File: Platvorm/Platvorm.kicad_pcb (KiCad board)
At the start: 2 copper layers, 40.3 x 80 mm, 38 parts, among them J1 Power Header 2x8, J2 GPIO 2x14, J3 USB-C, Q1 S8050, Q2 S8050, SW1 BOOT, SW2 RESET, U1 ESP32-C6-WROOM-1-N8, U2 TPS54202DDCR, U3 USBLC6-2SC6, U4 CH340C

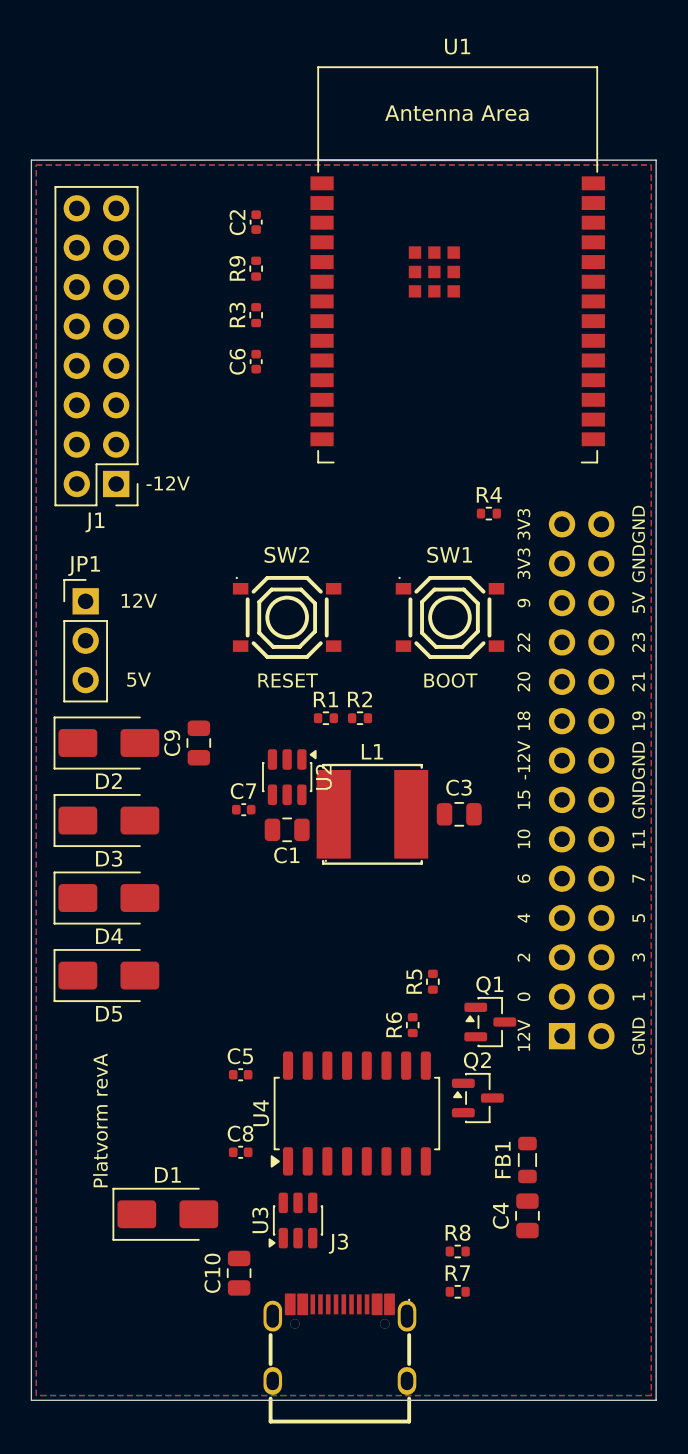
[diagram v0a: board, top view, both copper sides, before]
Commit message: Route board: DRC 0 violations, 0 unconnected
- freerouting pass (127 nets) + hand-finished stragglers:
  +5V to J2.24 (B.Cu row-band approach), IO22, +12V to JP1.1
  (via-hop x=56.6), +12V_RAW rerouted east (x=57.34), +5V west
  re-feed via B.Cu, CC lines, J3 GND tab bridges, C3 GND stitch via
- Default netclass clearance 0.2 -> 0.15mm (JLC 2-layer capability
  is 0.09mm; unlocks east-column lane capacity for J2 fanout)
- min_resolved_spokes 2 -> 1: four PTH GND pads (J2.14/28, J3 tabs)
  connect via 1 thermal spoke + PTH barrel + verified track ties
- Known deviation: SW node uses 2 vias + 5mm B.Cu jumper under U2
  (F.Cu corridor blocked by GND/FB/VOUT_PRE walls; ~4nH added loop
  inductance, acceptable at 500kHz with spread-spectrum TPS54202)
- Final: 576 tracks, 66 vias, 2013mm total, EN 69mm (was 103),
  IO9 67mm (was 85), GND pours filled both layers
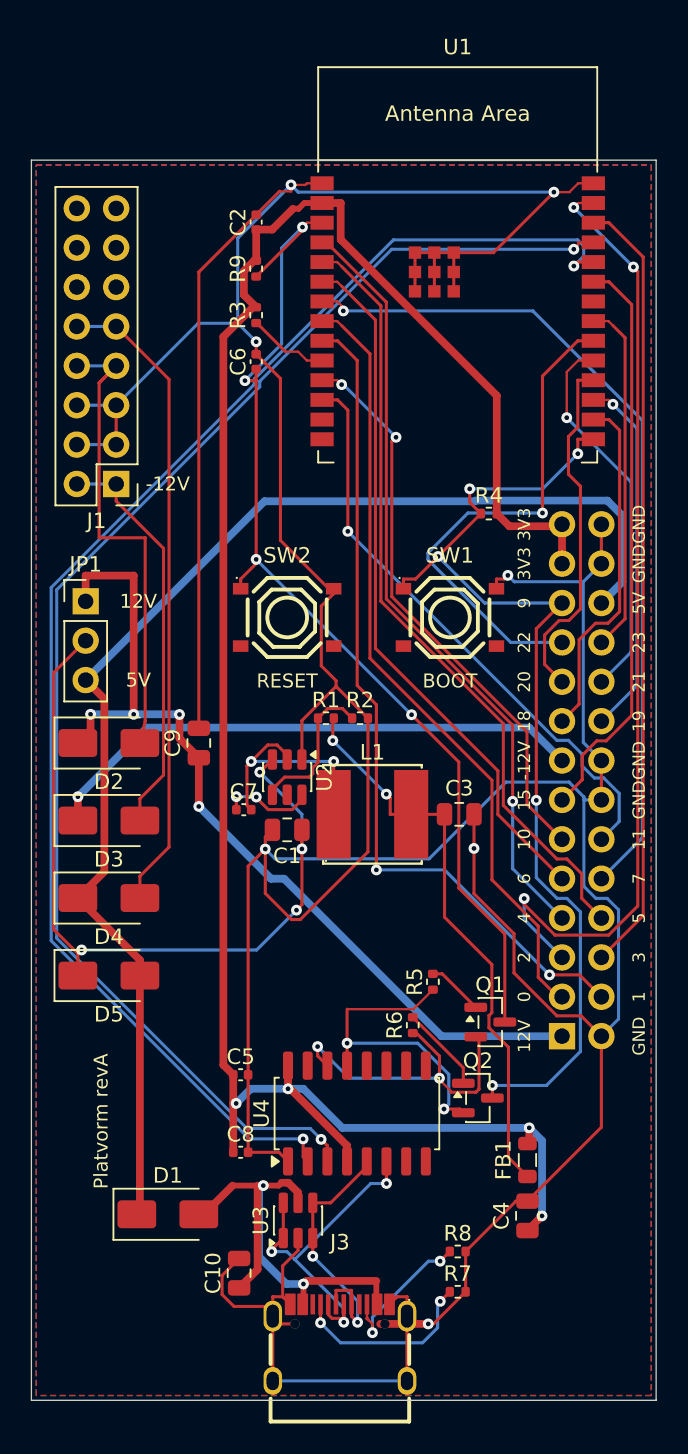
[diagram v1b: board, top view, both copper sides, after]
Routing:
- net GND: track 0.00 -> 333.0 mm, vias 0 -> 7
- net +3V3: track 0.00 -> 135.7 mm, vias 0 -> 4
- net U0RXD: track 0.00 -> 92.8 mm, vias 0 -> 2
- net U0TXD: track 0.00 -> 90.7 mm, vias 0 -> 2
- net +5V: track 0.00 -> 83.4 mm
- net EN: track 0.00 -> 69.0 mm, vias 0 -> 4
- net IO9: track 0.00 -> 66.9 mm, vias 0 -> 5
- net IO2: track 0.00 -> 62.3 mm, vias 0 -> 3
- net +12V: track 0.00 -> 57.7 mm, vias 0 -> 4
- net IO7: track 0.00 -> 54.6 mm, vias 0 -> 1
- net IO1: track 0.00 -> 54.1 mm, vias 0 -> 2
- net /Power Supply/VIN_BUCK: track 0.00 -> 50.9 mm, vias 0 -> 4
- net IO0: track 0.00 -> 50.7 mm
- net IO5: track 0.00 -> 50.7 mm
- net IO3: track 0.00 -> 50.4 mm
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
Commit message: Fab fixes: J3 shield tab annular/clearance, IO8 track width
- J3 USB-C shield tabs: height 0.7->0.8mm (annular 0.15mm = board min),
  pad clearance 0.1->0.2mm; clears 2 annular-width + 6 plane-clearance
  DRC errors against the +3V3 plane
- IO8 track: 0.1875->0.2mm; clears connection-width neck at U1.10
- 24 unconnected nets remain (routing WIP); DRC report in DRC5.rpt
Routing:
- net GND: track 333.0 -> 30.4 mm, vias 7 -> 28
- net +3V3: track 135.7 -> 10.5 mm, vias 4 -> 10
- net +5V: track 83.4 -> 160.2 mm, vias 0 -> 10
- net IO4: track 50.2 -> 1.80 mm
- net IO11: track 38.1 -> 0.00 mm, vias 1 -> 0
- net /Power Supply/VOUT_PRE: track 37.0 -> 7.90 mm
- net IO6: track 45.5 -> 70.9 mm, vias 0 -> 8
- net IO10: track 36.9 -> 60.6 mm, vias 2 -> 15
- net IO21: track 24.5 -> 1.80 mm
- net IO19: track 23.4 -> 1.80 mm
- net IO15: track 37.3 -> 57.3 mm, vias 0 -> 6
- net U0RXD: track 92.8 -> 75.3 mm, vias 2 -> 10
- net VBUS: track 31.2 -> 14.8 mm
- net /Power Supply/VIN_BUCK: track 50.9 -> 36.9 mm, vias 4 -> 3
- net IO18: track 22.8 -> 35.5 mm, vias 0 -> 7
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- added copper zone on In2.Cu, net +3V3
- added copper zone on In1.Cu, net GND
- removed copper zone on B.Cu, net GND
- removed copper zone on F.Cu, net GND
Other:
- copper layers 2 -> 4

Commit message: Update Platvorm board and project settings
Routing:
- net +3V3: track 10.5 -> 17.5 mm
- net /Power Supply/+12V_RAW: track 25.3 -> 28.2 mm
- net IO15: track 57.3 -> 58.1 mm
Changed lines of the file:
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@@
 	)
 	(segment
+		(start 66.555 109.1125)
+		(end 70.365 112.9225)
+		(width 0.45)
+		(layer "F.Cu")
+		(net "+3V3")
+	)
+	(segment
 		(start 64.5 59.49)
 		(end 63.7 58.69)
@@
 	)
 	(segment
+		(start 70.365 112.9225)
+		(end 70.365 114.5875)
+		(width 0.45)
+		(layer "F.Cu")
+		(net "+3V3")
+	)
+	(segment
 		(start 82 113.4375)
 		(end 82.9 114.3375)
@@
 	)
 	(segment
-		(start 51.325 59.875)
-		(end 51.325 72.525)
+		(start 53.775 99.275)
+		(end 53.775 98.025)
 		(width 1)
 		(layer "F.Cu")
@@
 	)
 	(segment
-		(start 53.775 99.275)
-		(end 53.775 98.025)
+		(start 52.575 72.525)
+		(end 51.525 72.525)
 		(width 1)
 		(layer "F.Cu")
@@
 	)
 	(segment
-		(start 51.325 72.525)
-		(end 52.575 72.525)
+		(start 51.325 72.325)
+		(end 51.325 59.875)
+		(width 1)
+		(layer "F.Cu")
+		(net "+5V")
+	)
+	(segment
+		(start 51.525 72.525)
+		(end 51.325 72.325)
 		(width 1)
 		(layer "F.Cu")
@@
 	)
 	(segment
-		(start 55.925 63.925)
-		(end 55.925 64.175)
+		(start 58.5 72.5)
+		(end 58.5 64.5)
 		(width 1)
 		(layer "F.Cu")
@@
 	)
 	(segment
-		(start 55.925 64.175)
-		(end 57.075 64.175)
+		(start 57.27 63.27)
+		(end 55.47 63.27)
 		(width 1)
 		(layer "F.Cu")
@@
 	)
 	(segment
-		(start 54.675 63.225)
-		(end 53.725 63.225)
+		(start 57 87.6)
+		(end 57 74)
 		(width 1)
 		(layer "F.Cu")
@@
 	)
 	(segment
-		(start 57.075 64.175)
-		(end 57.075 87.125)
+		(start 58.5 64.5)
+		(end 57.27 63.27)
+		(width 1)
+		(layer "F.Cu")
+		(net "/Power Supply/+12V_RAW")
+	)
+	(segment
+		(start 57 74)
+		(end 58.5 72.5)
+		(width 1)
+		(layer "F.Cu")
+		(net "/Power Supply/+12V_RAW")
+	)
+	(segment
+		(start 54.675 63.225)
+		(end 53.725 63.225)
 		(width 1)
 		(layer "F.Cu")
@@
 	)
 	(segment
+		(start 70.365 108.4125)
+		(end 70.365 109.324999)
+		(width 0.2)
+		(layer "F.Cu")
+		(net "/USB & UART Bridge/DTR")
+	)
+	(segment
 		(start 70.525 107.675)
 		(end 70.525 103.625)
@@
 	)
 	(segment
-		(start 70.525 111.275)
-		(end 77.275 111.275)
+		(start 72.490001 111.45)
+		(end 77.8625 111.45)
 		(width 0.2)
 		(layer "F.Cu")
@@
 	)
 	(segment
-		(start 70.525 109.175)
-		(end 70.525 111.275)
+		(start 70.365 109.324999)
+		(end 72.490001 111.45)
 		(width 0.2)
 		(layer "F.Cu")
@@
 	)
 	(segment
-		(start 65.175 61.875)
-		(end 64.675 61.875)
-		(width 0.2)
+		(start 68.75 62.925)
+		(end 66.915 62.925)
+		(width 0.25)
 		(layer "F.Cu")
 		(net "/ESP32-C6 Module/IO8")
 	)
 	(segment
-		(start 65.175 62.525)
-		(end 65.175 61.875)
-		(width 0.2)
-		(layer "F.Cu")
-		(net "/ESP32-C6 Module/IO8")
-	)
-	(segment
-		(start 68.025 62.525)
-		(end 65.175 62.525)
-		(width 0.2)
-		(layer "F.Cu")
-		(net "/ESP32-C6 Module/IO8")
-	)
-	(segment
-		(start 64.675 61.875)
-		(end 64.675 60.625)
-		(width 0.2)
+		(start 66.915 62.925)
+		(end 64.5 60.51)
+		(width 0.25)
 		(layer "F.Cu")
 		(net "/ESP32-C6 Module/IO8")
@@
 	)
 	(segment
+		(start 80.555 57.845)
+		(end 80.175 58.225)
+		(width 0.25)
+		(layer "F.Cu")
+		(net "IO15")
+	)
+	(segment
 		(start 76.975 70.775)
 		(end 76.975 74.575)
@@
 	)
 	(segment
-		(start 85.525 58.225)
-		(end 80.175 58.225)
-		(width 0.2)
-		(layer "F.Cu")
-		(net "IO15")
-	)
-	(segment
 		(start 78.725 90.925)
 		(end 81.125 90.925)
@@
 		(layer "F.Cu")
 		(net "IO15")
+	)
+	(segment
+		(start 86.25 57.845)
+		(end 80.555 57.845)
+		(width 0.25)
+		(layer "F.Cu")
+		(net "IO15")
